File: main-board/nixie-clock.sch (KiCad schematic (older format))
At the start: 19 parts, among them P1 ESP8266_CONN, U1 STM32F103CBT6, Y1 32.768kHz

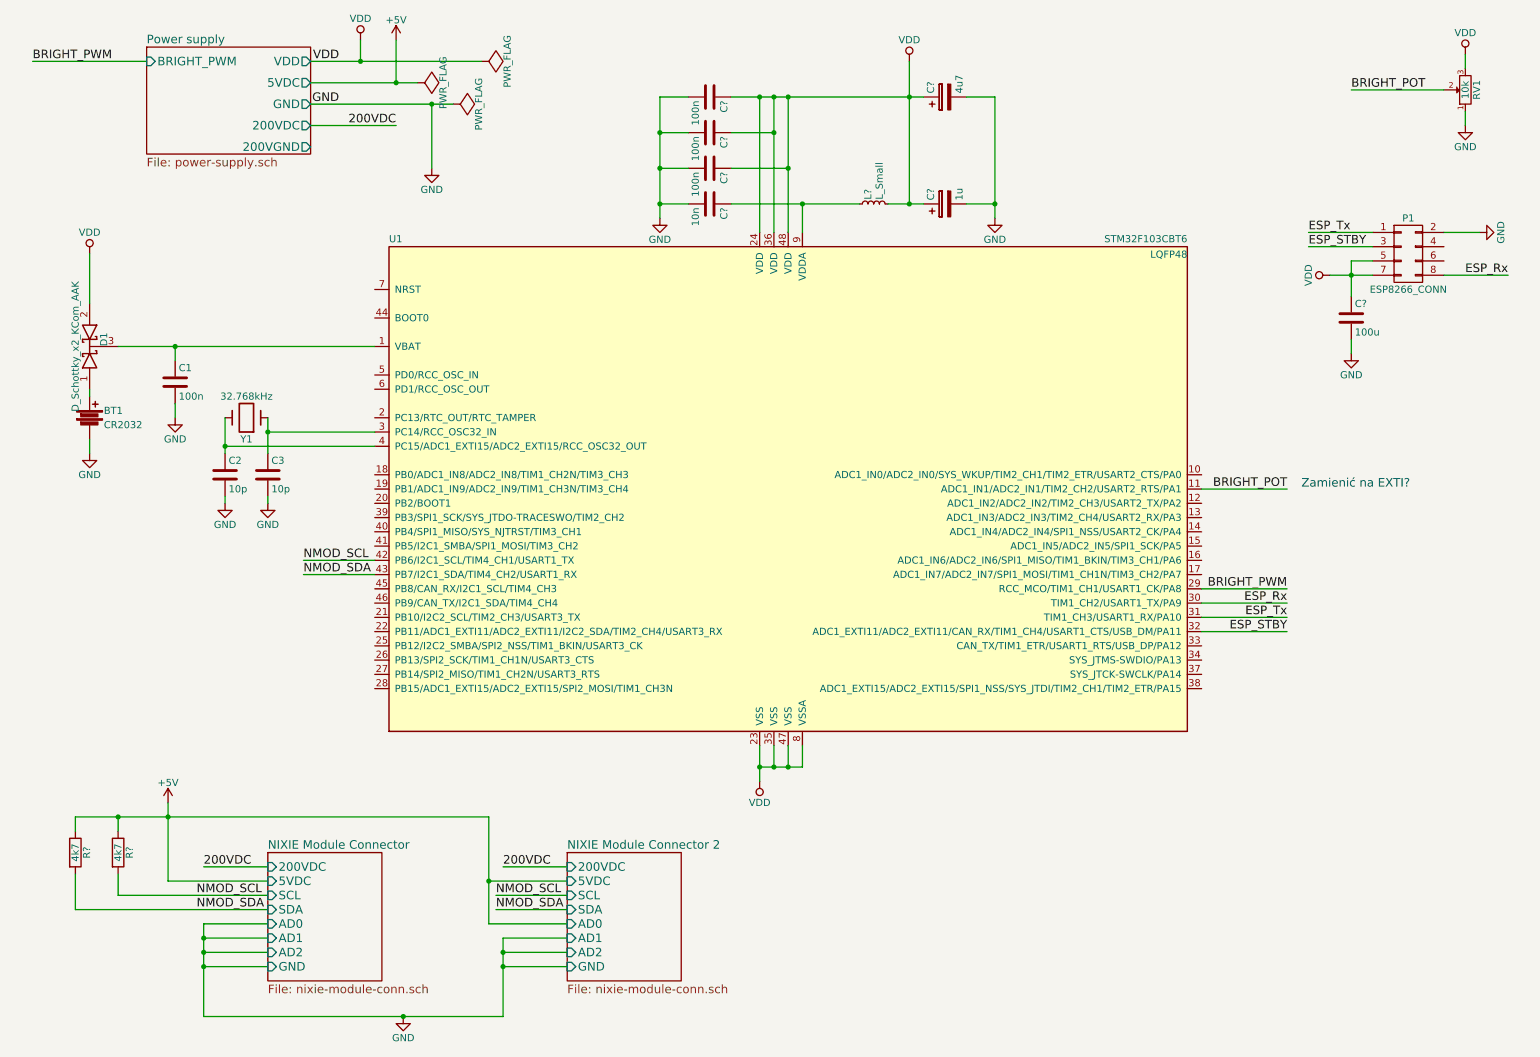
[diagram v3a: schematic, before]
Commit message: Poprawka zasilania stm32 i esp; VSS-GND
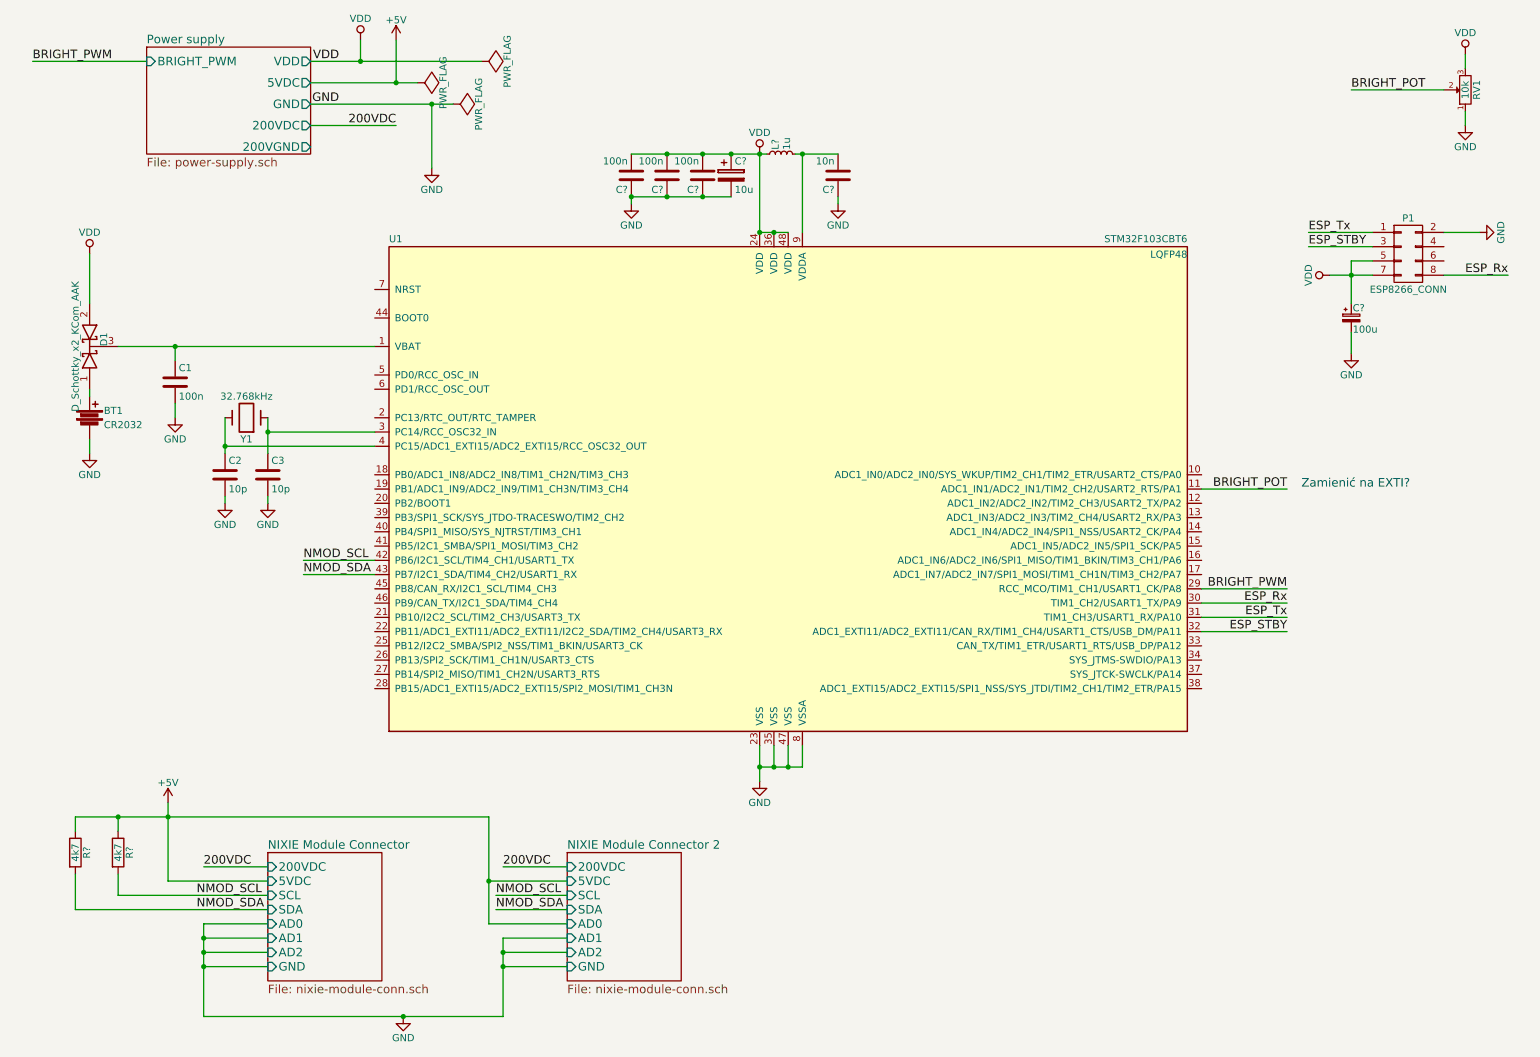
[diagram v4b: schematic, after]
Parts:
- removed C?: 100u, symbol C
- removed C?: 1u, symbol CP
- added C?: 100u, symbol CP_Small
- C?: value 4u7 -> 10u
- L?: value L_Small -> 1u
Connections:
- net GND: now also C?.1, C?.1, C?.1, C?.1, U1.23 (VSS), U1.35 (VSS), U1.47 (VSS), U1.8 (VSSA), C?.2; no longer C?.2, C?.2, C?.2, C?.2
- net VDD: now also C?.2, C?.2, C?.2, L?.1, C?.1; no longer C?.1, C?.1, C?.1, L?.2, U1.23 (VSS), U1.35 (VSS), U1.47 (VSS), U1.8 (VSSA)
- new net: C?.2, L?.2, U1.9 (VDDA)
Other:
- moved on the sheet: C?, L?
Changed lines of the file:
@@
 L VDD #PWR010
 U 1 1 58176451
-P 6850 850
-F 0 "#PWR010" H 6850 700 50  0001 C CNN
-F 1 "VDD" H 6850 1000 50  0000 C CNN
-F 2 "" H 6850 850 50  0000 C CNN
-F 3 "" H 6850 850 50  0000 C CNN
-	1    6850 850
-	1    0    0    -1
-$EndComp
-$Comp
-L VDD #PWR011
-U 1 1 58176B17
-P 5800 5900
-F 0 "#PWR011" H 5800 5750 50  0001 C CNN
-F 1 "VDD" H 5800 6050 50  0000 C CNN
-F 2 "" H 5800 5900 50  0000 C CNN
-F 3 "" H 5800 5900 50  0000 C CNN
-	1    5800 5900
-	-1   0    0    1
+P 5800 1500
+F 0 "#PWR010" H 5800 1350 50  0001 C CNN
+F 1 "VDD" H 5800 1650 50  0000 C CNN
+F 2 "" H 5800 1500 50  0000 C CNN
+F 3 "" H 5800 1500 50  0000 C CNN
+	1    5800 1500
+	1    0    0    -1
 $EndComp
 Connection ~ 3000 850
@@
 	9800 2350 10100 2350
 Wire Wire Line
-	9950 2250 9950 2500
+	9950 2250 9950 2550
 Wire Wire Line
 	9950 2250 10100 2250
@@
 Connection ~ 1300 6150
 $Comp
-L C C?
-U 1 1 5822ADBF
-P 9950 2650
-F 0 "C?" H 9975 2750 50  0000 L CNN
-F 1 "100u" H 9975 2550 50  0000 L CNN
-F 2 "" H 9988 2500 50  0000 C CNN
-F 3 "" H 9950 2650 50  0000 C CNN
-	1    9950 2650
-	1    0    0    -1
-$EndComp
-$Comp
 L GND #PWR?
 U 1 1 5822B6A3
@@
 $EndComp
 Wire Wire Line
-	9950 2800 9950 2900
-Wire Wire Line
-	6850 850  6850 1850
-Wire Wire Line
-	6700 1850 6950 1850
+	9950 2750 9950 2900
 $Comp
 L L_Small L?
 U 1 1 5823D1D2
-P 6600 1850
-F 0 "L?" H 6630 1890 50  0000 L CNN
-F 1 "L_Small" H 6630 1810 50  0000 L CNN
-F 2 "" H 6600 1850 50  0000 C CNN
-F 3 "" H 6600 1850 50  0000 C CNN
-	1    6600 1850
+P 5950 1500
+F 0 "L?" H 5980 1540 50  0000 L CNN
+F 1 "1u" H 5980 1460 50  0000 L CNN
+F 2 "" H 5950 1500 50  0000 C CNN
+F 3 "" H 5950 1500 50  0000 C CNN
+	1    5950 1500
 	0    -1   -1   0
 $EndComp
@@
 L C C?
 U 1 1 5823DB5F
-P 5450 1100
-F 0 "C?" H 5475 1200 50  0000 L CNN
-F 1 "100n" H 5475 1000 50  0000 L CNN
-F 2 "" H 5488 950 50  0000 C CNN
-F 3 "" H 5450 1100 50  0000 C CNN
-	1    5450 1100
-	0    1    1    0
+P 4900 1650
+F 0 "C?" H 4925 1750 50  0000 L CNN
+F 1 "100n" H 4925 1550 50  0000 L CNN
+F 2 "" H 4938 1500 50  0000 C CNN
+F 3 "" H 4900 1650 50  0000 C CNN
+	1    4900 1650
+	-1   0    0    1
 $EndComp
 $Comp
 L C C?
 U 1 1 5823DCA3
-P 5450 1350
-F 0 "C?" H 5475 1450 50  0000 L CNN
-F 1 "100n" H 5475 1250 50  0000 L CNN
-F 2 "" H 5488 1200 50  0000 C CNN
-F 3 "" H 5450 1350 50  0000 C CNN
-	1    5450 1350
-	0    1    1    0
+P 5150 1650
+F 0 "C?" H 5175 1750 50  0000 L CNN
+F 1 "100n" H 5175 1550 50  0000 L CNN
+F 2 "" H 5188 1500 50  0000 C CNN
+F 3 "" H 5150 1650 50  0000 C CNN
+	1    5150 1650
+	-1   0    0    1
 $EndComp
 $Comp
 L C C?
 U 1 1 5823DDC2
-P 5450 1600
-F 0 "C?" H 5475 1700 50  0000 L CNN
-F 1 "100n" H 5475 1500 50  0000 L CNN
-F 2 "" H 5488 1450 50  0000 C CNN
-F 3 "" H 5450 1600 50  0000 C CNN
-	1    5450 1600
-	0    1    1    0
+P 5400 1650
+F 0 "C?" H 5425 1750 50  0000 L CNN
+F 1 "100n" H 5425 1550 50  0000 L CNN
+F 2 "" H 5438 1500 50  0000 C CNN
+F 3 "" H 5400 1650 50  0000 C CNN
+	1    5400 1650
+	-1   0    0    1
 $EndComp
 $Comp
 L C C?
 U 1 1 5823DE92
-P 5450 1850
-F 0 "C?" H 5475 1950 50  0000 L CNN
-F 1 "10n" H 5475 1750 50  0000 L CNN
-F 2 "" H 5488 1700 50  0000 C CNN
-F 3 "" H 5450 1850 50  0000 C CNN
-	1    5450 1850
-	0    1    1    0
-$EndComp
-Wire Wire Line
-	5600 1850 6500 1850
-Wire Wire Line
-	6100 1850 6100 2050
-Wire Wire Line
-	5600 1100 6950 1100
-Wire Wire Line
-	6000 1100 6000 2050
-Connection ~ 6850 1100
-Wire Wire Line
-	5900 1100 5900 2050
-Connection ~ 6000 1100
-Wire Wire Line
-	5800 1100 5800 2050
-Connection ~ 5900 1100
-Connection ~ 5800 1100
-Wire Wire Line
-	5900 1350 5600 1350
-Connection ~ 5900 1350
-Wire Wire Line
-	6000 1600 5600 1600
-Connection ~ 6000 1600
-Connection ~ 6100 1850
+P 6350 1650
+F 0 "C?" H 6375 1750 50  0000 L CNN
+F 1 "10n" H 6375 1550 50  0000 L CNN
+F 2 "" H 6388 1500 50  0000 C CNN
+F 3 "" H 6350 1650 50  0000 C CNN
+	1    6350 1650
+	-1   0    0    1
+$EndComp
 $Comp
 L GND #PWR?
 U 1 1 5823EC3A
-P 5100 1950
-F 0 "#PWR?" H 5100 1700 50  0001 C CNN
-F 1 "GND" H 5100 1800 50  0000 C CNN
-F 2 "" H 5100 1950 50  0000 C CNN
-F 3 "" H 5100 1950 50  0000 C CNN
-	1    5100 1950
-	1    0    0    -1
-$EndComp
-Wire Wire Line
-	5300 1100 5100 1100
-Wire Wire Line
-	5100 1100 5100 1950
-Wire Wire Line
-	5100 1350 5300 1350
-Connection ~ 5100 1350
-Wire Wire Line
-	5100 1600 5300 1600
-Connection ~ 5100 1600
-Wire Wire Line
-	5100 1850 5300 1850
-Connection ~ 5100 1850
+P 4900 1850
+F 0 "#PWR?" H 4900 1600 50  0001 C CNN
+F 1 "GND" H 4900 1700 50  0000 C CNN
+F 2 "" H 4900 1850 50  0000 C CNN
+F 3 "" H 4900 1850 50  0000 C CNN
+	1    4900 1850
+	1    0    0    -1
+$EndComp
 $Comp
 L CP C?
 U 1 1 5824062E
-P 7100 1100
-F 0 "C?" H 7125 1200 50  0000 L CNN
-F 1 "4u7" H 7125 1000 50  0000 L CNN
-F 2 "" H 7138 950 50  0000 C CNN
-F 3 "" H 7100 1100 50  0000 C CNN
-	1    7100 1100
-	0    -1   -1   0
-$EndComp
-$Comp
-L CP C?
-U 1 1 582407B1
-P 7100 1850
-F 0 "C?" H 7125 1950 50  0000 L CNN
-F 1 "1u" H 7125 1750 50  0000 L CNN
-F 2 "" H 7138 1700 50  0000 C CNN
-F 3 "" H 7100 1850 50  0000 C CNN
-	1    7100 1850
-	0    -1   -1   0
-$EndComp
-Connection ~ 6850 1850
+P 5600 1650
+F 0 "C?" H 5625 1750 50  0000 L CNN
+F 1 "10u" H 5625 1550 50  0000 L CNN
+F 2 "" H 5638 1500 50  0000 C CNN
+F 3 "" H 5600 1650 50  0000 C CNN
+	1    5600 1650
+	1    0    0    -1
+$EndComp
 $Comp
 L GND #PWR?
 U 1 1 58241A1B
-P 7450 1950
-F 0 "#PWR?" H 7450 1700 50  0001 C CNN
-F 1 "GND" H 7450 1800 50  0000 C CNN
-F 2 "" H 7450 1950 50  0000 C CNN
-F 3 "" H 7450 1950 50  0000 C CNN
-	1    7450 1950
-	1    0    0    -1
-$EndComp
-Wire Wire Line
-	7250 1100 7450 1100
-Wire Wire Line
-	7450 1100 7450 1950
-Wire Wire Line
-	7250 1850 7450 1850
-Connection ~ 7450 1850
+P 6350 1850
+F 0 "#PWR?" H 6350 1600 50  0001 C CNN
+F 1 "GND" H 6350 1700 50  0000 C CNN
+F 2 "" H 6350 1850 50  0000 C CNN
+F 3 "" H 6350 1850 50  0000 C CNN
+	1    6350 1850
+	1    0    0    -1
+$EndComp
+$Comp
+L CP_Small C?
+U 1 1 5821B579
+P 9950 2650
+F 0 "C?" H 9960 2720 50  0000 L CNN
+F 1 "100u" H 9960 2570 50  0000 L CNN
+F 2 "" H 9950 2650 50  0000 C CNN
+F 3 "" H 9950 2650 50  0000 C CNN
+	1    9950 2650
+	1    0    0    -1
+$EndComp
+Wire Wire Line
+	5800 2050 6000 2050
+Wire Wire Line
+	5800 1500 5800 2050
+Wire Wire Line
+	4900 1500 5850 1500
+Connection ~ 5150 1500
+Connection ~ 5400 1500
+Connection ~ 5800 1500
+Connection ~ 5800 2050
+Connection ~ 5900 2050
+Wire Wire Line
+	4900 1800 5600 1800
+Wire Wire Line
+	4900 1800 4900 1850
+Connection ~ 4900 1800
+Connection ~ 5150 1800
+Wire Wire Line
+	6350 1850 6350 1800
+Wire Wire Line
+	6050 1500 6350 1500
+Wire Wire Line
+	6100 2050 6100 1500
+Connection ~ 6100 1500
+Connection ~ 5400 1800
+Connection ~ 5600 1500
+$Comp
+L GND #PWR?
+U 1 1 5822205E
+P 5800 5900
+F 0 "#PWR?" H 5800 5650 50  0001 C CNN
+F 1 "GND" H 5800 5750 50  0000 C CNN
+F 2 "" H 5800 5900 50  0000 C CNN
+F 3 "" H 5800 5900 50  0000 C CNN
+	1    5800 5900
+	1    0    0    -1
+$EndComp
 $EndSCHEMATC

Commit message: #1 - enkoder zamiast potencjometru; pomiar napiecia zarzenia; SWD; BOOT0 do masy
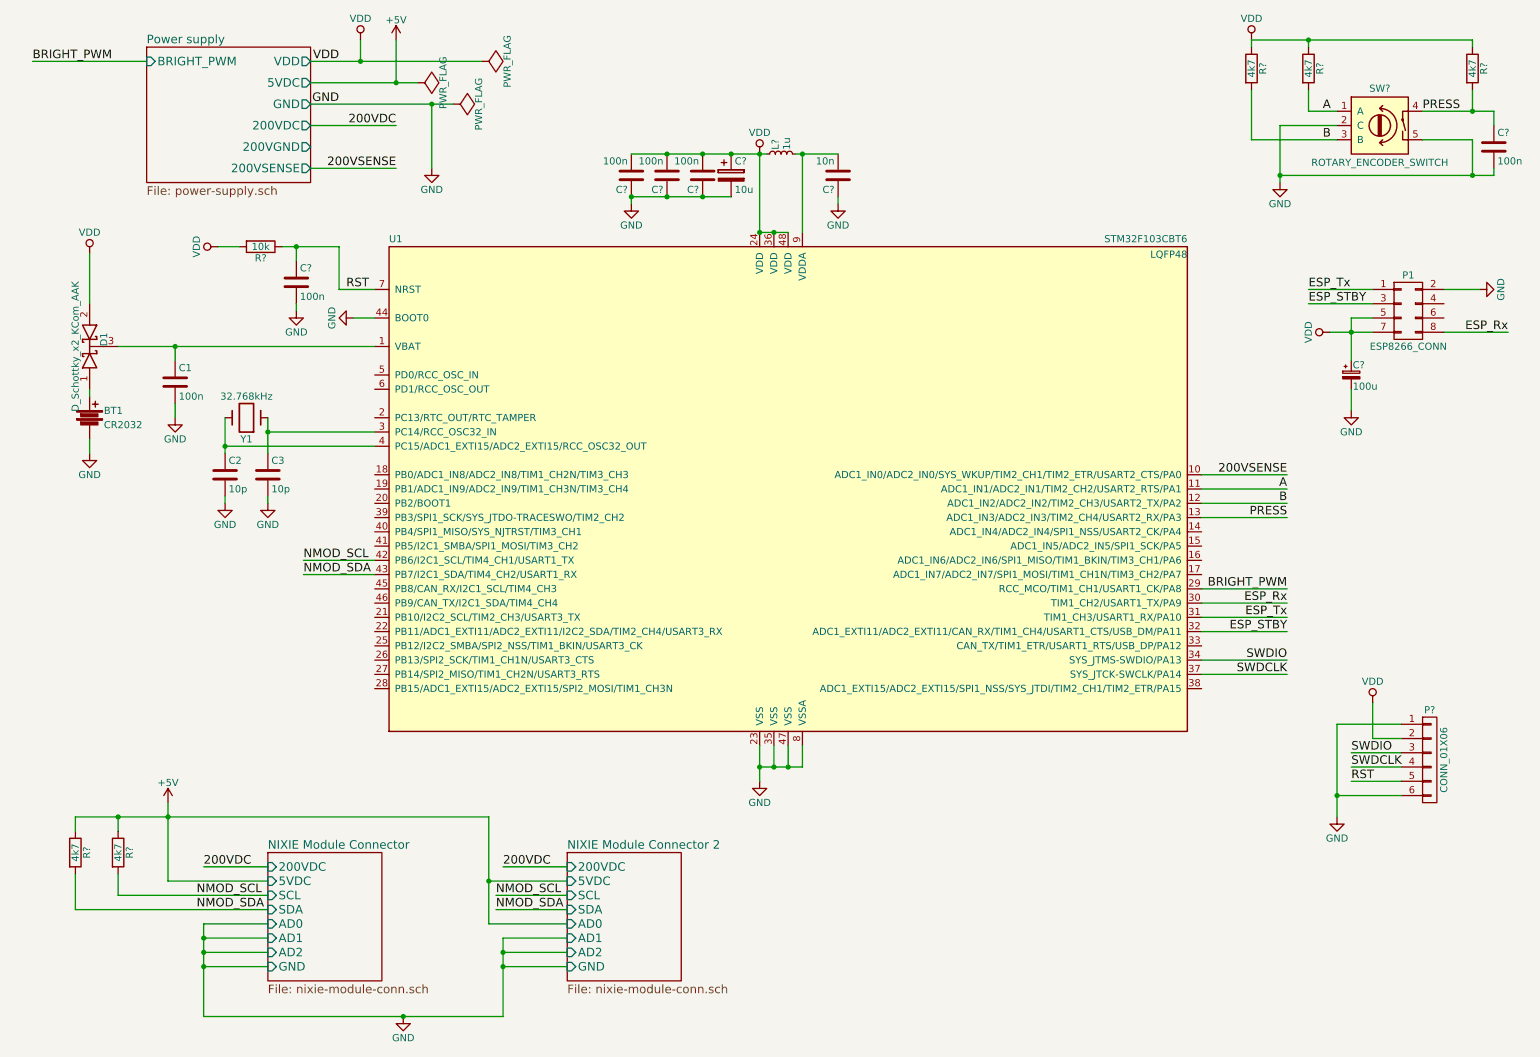
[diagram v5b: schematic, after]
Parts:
- removed RV1: 10k, symbol POT
- added C? (x2): 100n, symbol C
- added P?: CONN_01X06, symbol CONN_01X06
- added R? (x3): 4k7, symbol R
- added R?: 10k, symbol R
- added SW?: ROTARY_ENCODER_SWITCH, symbol ROTARY_ENCODER_SWITCH
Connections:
- net GND: now also U1.44 (BOOT0), C?.2, C?.2, P?.1 (P1), P?.6 (P6), SW?.2 (C), SW?.5
- net VDD: now also P?.2 (P2), R?.1, R?.1, R?.1, R?.2
- net 200VSENSE: now reaches U1.10 (ADC1_IN0/ADC2_IN0/SYS_WKUP/TIM2_CH1/TIM2_ETR/USART2_CTS/PA0)
- net B: now reaches U1.12 (ADC1_IN2/ADC2_IN2/TIM2_CH3/USART2_TX/PA2)
- net B: now also R?.2, SW?.3 (B)
- net PRESS: now reaches U1.13 (ADC1_IN3/ADC2_IN3/TIM2_CH4/USART2_RX/PA3)
- net PRESS: now also C?.1, R?.2, SW?.4
- net SWDIO: now reaches U1.34 (SYS_JTMS-SWDIO/PA13)
- net SWDIO: now also P?.3 (P3)
- net SWDCLK: now reaches U1.37 (SYS_JTCK-SWCLK/PA14)
- net SWDCLK: now also P?.4 (P4)
- net RST: now reaches U1.7 (NRST)
- net RST: now also C?.1, P?.5 (P5), R?.1
- net BRIGHT_POT renamed A
- net A: now also R?.2, SW?.1 (A)
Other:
- note removed: "Zamienić na EXTI?"
- moved on the sheet: C?, P1
